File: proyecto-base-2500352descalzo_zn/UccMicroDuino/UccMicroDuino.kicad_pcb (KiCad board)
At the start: 2 copper layers, 8 parts, among them J1 Conn_01x10_Socket, J2 USB_A, U1 ATtiny85-20S

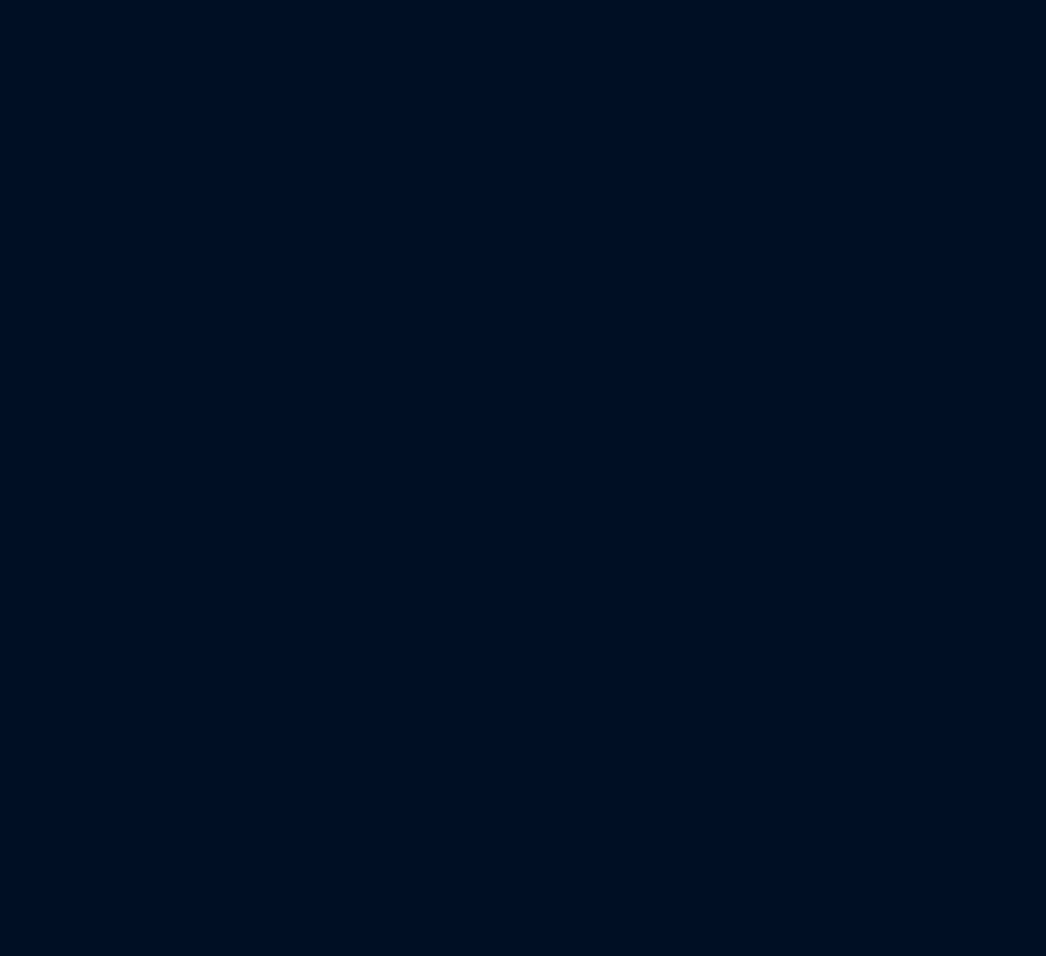
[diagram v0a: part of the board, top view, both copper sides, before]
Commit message: PLACA EDITADA EN LA ESQUINA
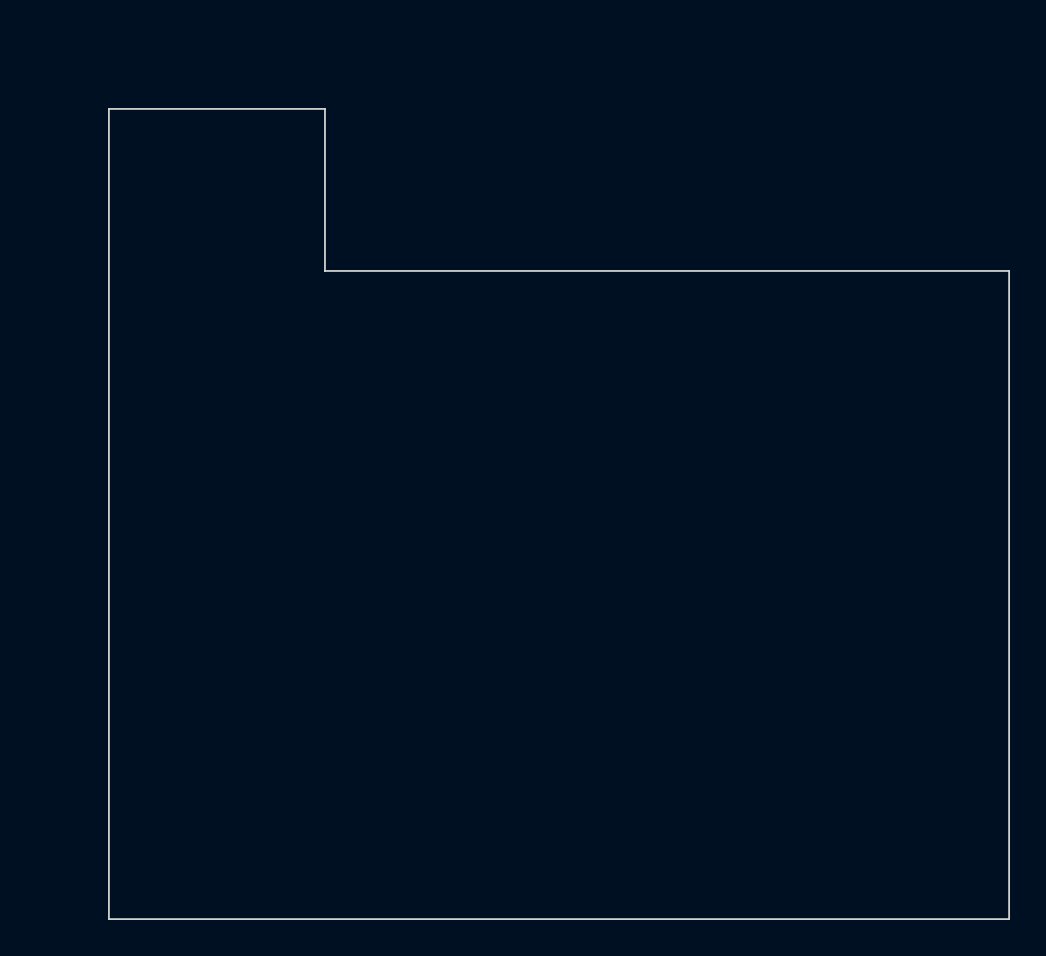
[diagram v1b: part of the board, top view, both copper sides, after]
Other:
- board outline added: 50 x 45 mm
